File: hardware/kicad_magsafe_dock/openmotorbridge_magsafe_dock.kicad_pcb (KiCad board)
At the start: 2 copper layers, 26 x 11.5 mm, 6 parts, among them J1 M8_6P_WIRE_PADS, J2 MAGSAFE_6P_DOCK, U1 USBLC6-4SC6

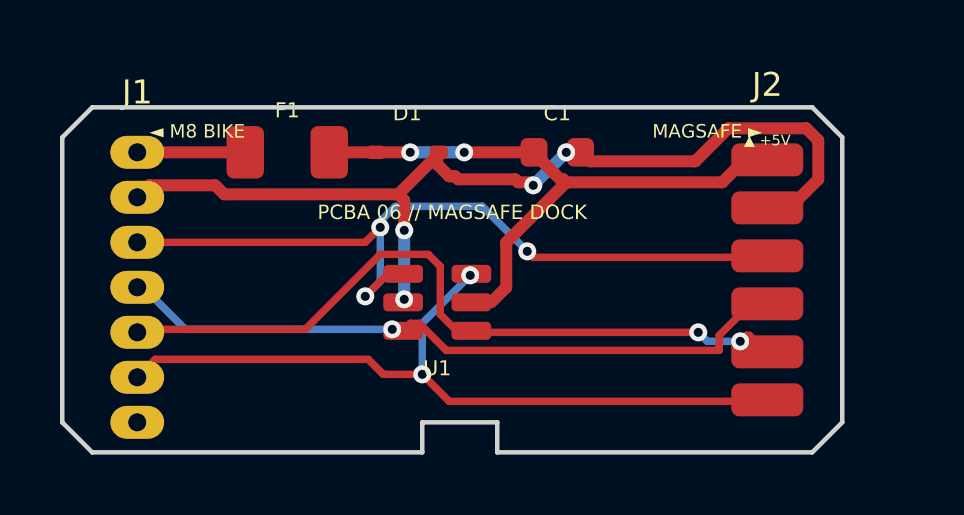
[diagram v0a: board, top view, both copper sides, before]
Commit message: feat(cad/pcb): redesign PCBA 06 and MagSafe frame dock enclosure with horizontal clamshell & central M2.5 boss
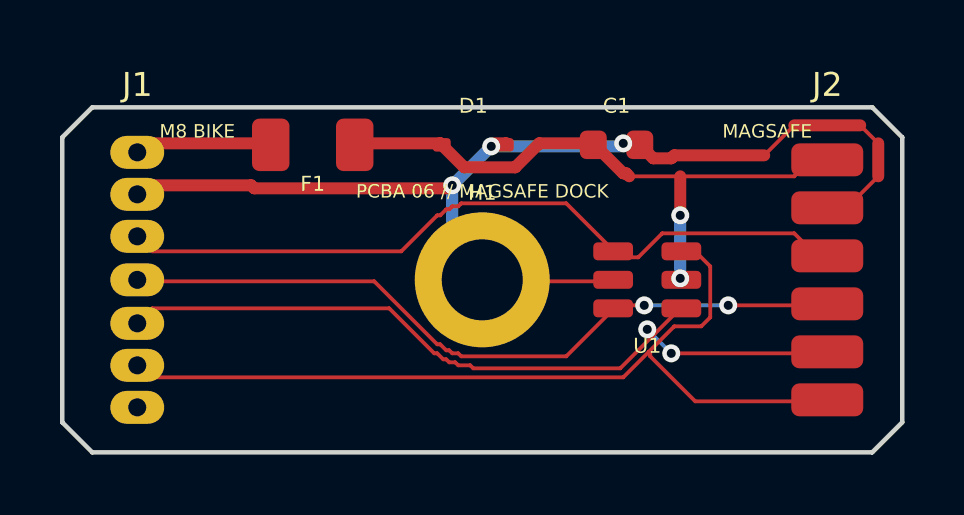
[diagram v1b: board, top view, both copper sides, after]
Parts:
- added H1: M2.5_MOUNT_HOLE, MountingHole:MountingHole_2.7mm_M2.5_Pad, F.Cu at (114.0, 75.8)
- moved U1 7.04 mm to (119.5, 75.8)
- moved D1 2.21 mm to (113.7, 71.2)
- moved J2 2.00 mm to (125.5, 75.8)
- moved C1 1.99 mm to (118.5, 71.2)
- moved F1 0.89 mm to (108.3, 71.2)
- moved J1 0.25 mm to (102.5, 75.8)
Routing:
- net GND: track 32.5 -> 37.6 mm, vias 4 -> 3
- net 1WIRE_ID: track 25.8 -> 29.8 mm, vias 2 -> 0
- net TRIGGER_PPS: track 24.5 -> 26.7 mm
- net SIG_N: track 22.8 -> 24.8 mm, vias 1 -> 2
- net SIG_P: track 26.5 -> 25.4 mm, vias 3 -> 0
- net VCC_IN: track 3.60 -> 4.27 mm
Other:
- board size 26 x 11.5 mm -> 28 x 11.5 mm
- board text added: "CENTER MOUNT M2.5 // IP67 DOCK"
- board text added: "M8 BIKE"
- board text added: "MAGSAFE"
- board text added: "OPENMOTORBRIDGE v8.2"
- board text removed: "ESD / PPTC PROTECTED DOCK"
- board text removed: "MAGSAFE ►"
- board text removed: "OPENMOTORBRIDGE v8.1"
- board text removed: "▲ +5V"
- board text removed: "◄ M8 BIKE"

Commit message: fix(pcb): provide 100% clean unrouted canvas for PCBA 06 awaiting manual routing
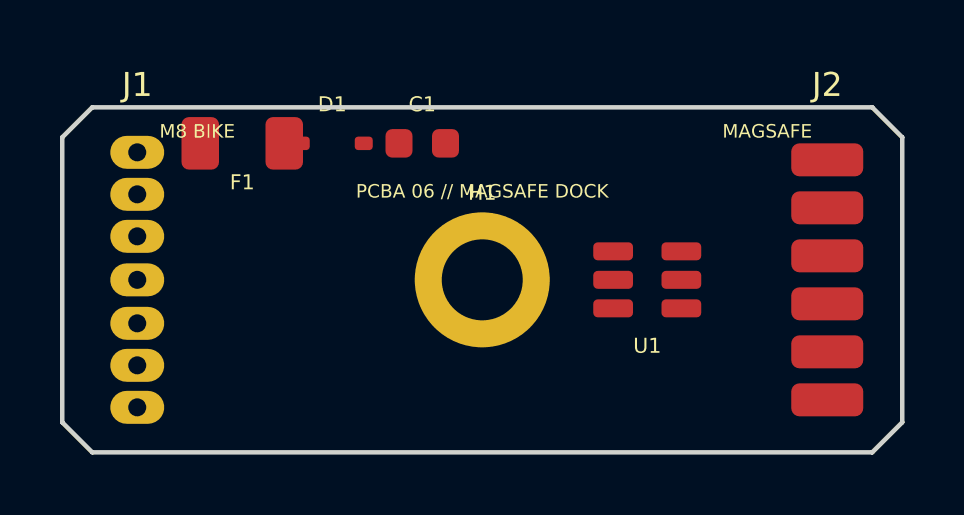
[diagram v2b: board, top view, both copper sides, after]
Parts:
- moved C1 6.48 mm to (112.0, 71.2)
- moved D1 4.70 mm to (109.0, 71.2)
- moved F1 2.35 mm to (106.0, 71.2)
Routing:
- net GND: track 37.6 -> 0.00 mm, vias 3 -> 0
- net 1WIRE_ID: track 29.8 -> 0.00 mm
- net TRIGGER_PPS: track 26.7 -> 0.00 mm, vias 2 -> 0
- net SIG_P: track 25.4 -> 0.00 mm
- net SIG_N: track 24.8 -> 0.00 mm, vias 2 -> 0
- net VCC_PROT: track 20.7 -> 0.00 mm, vias 2 -> 0
- net VCC_IN: track 4.27 -> 0.00 mm

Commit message: feat(pcba06): restore completed manual routing for PCBA 06 MagSafe dock
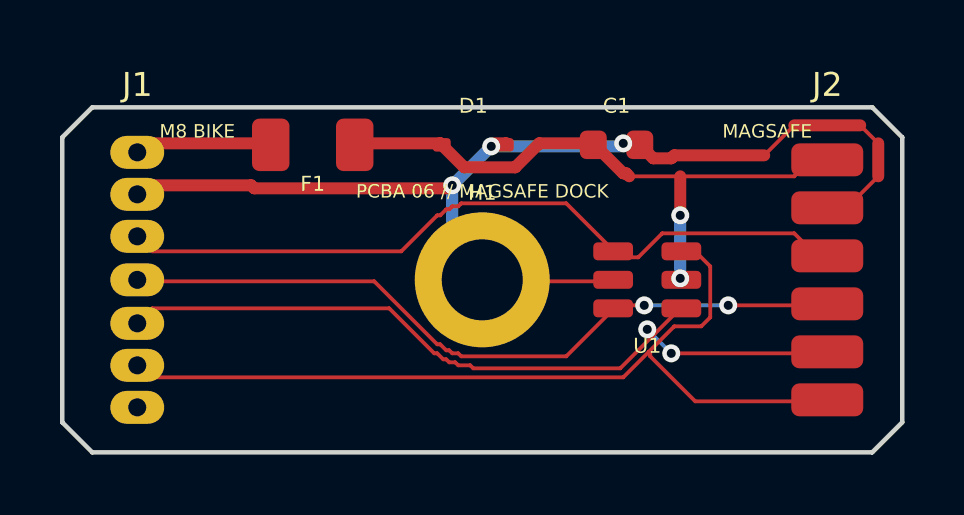
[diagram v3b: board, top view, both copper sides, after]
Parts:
- moved C1 6.48 mm to (118.5, 71.2)
- moved D1 4.70 mm to (113.7, 71.2)
- moved F1 2.35 mm to (108.3, 71.2)
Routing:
- net GND: track 0.00 -> 37.6 mm, vias 0 -> 3
- net 1WIRE_ID: track 0.00 -> 29.8 mm
- net TRIGGER_PPS: track 0.00 -> 26.7 mm, vias 0 -> 2
- net SIG_P: track 0.00 -> 25.4 mm
- net SIG_N: track 0.00 -> 24.8 mm, vias 0 -> 2
- net VCC_PROT: track 0.00 -> 20.7 mm, vias 0 -> 2
- net VCC_IN: track 0.00 -> 4.27 mm
